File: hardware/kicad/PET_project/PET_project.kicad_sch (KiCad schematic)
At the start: 22 parts, among them J1 Conn_01x02_Socket, J2 Screw_Terminal_01x02, J3 Screw_Terminal_01x02, J4 Conn_01x02_Socket, J5 GY-GPSV2-NEO6M, J6 BMM350, J7 MPU6050, J8 Conn_01x02_Socket, J9 BMP280, Q2 NMOS, Q3 NMOS, U8 BA50DD0T

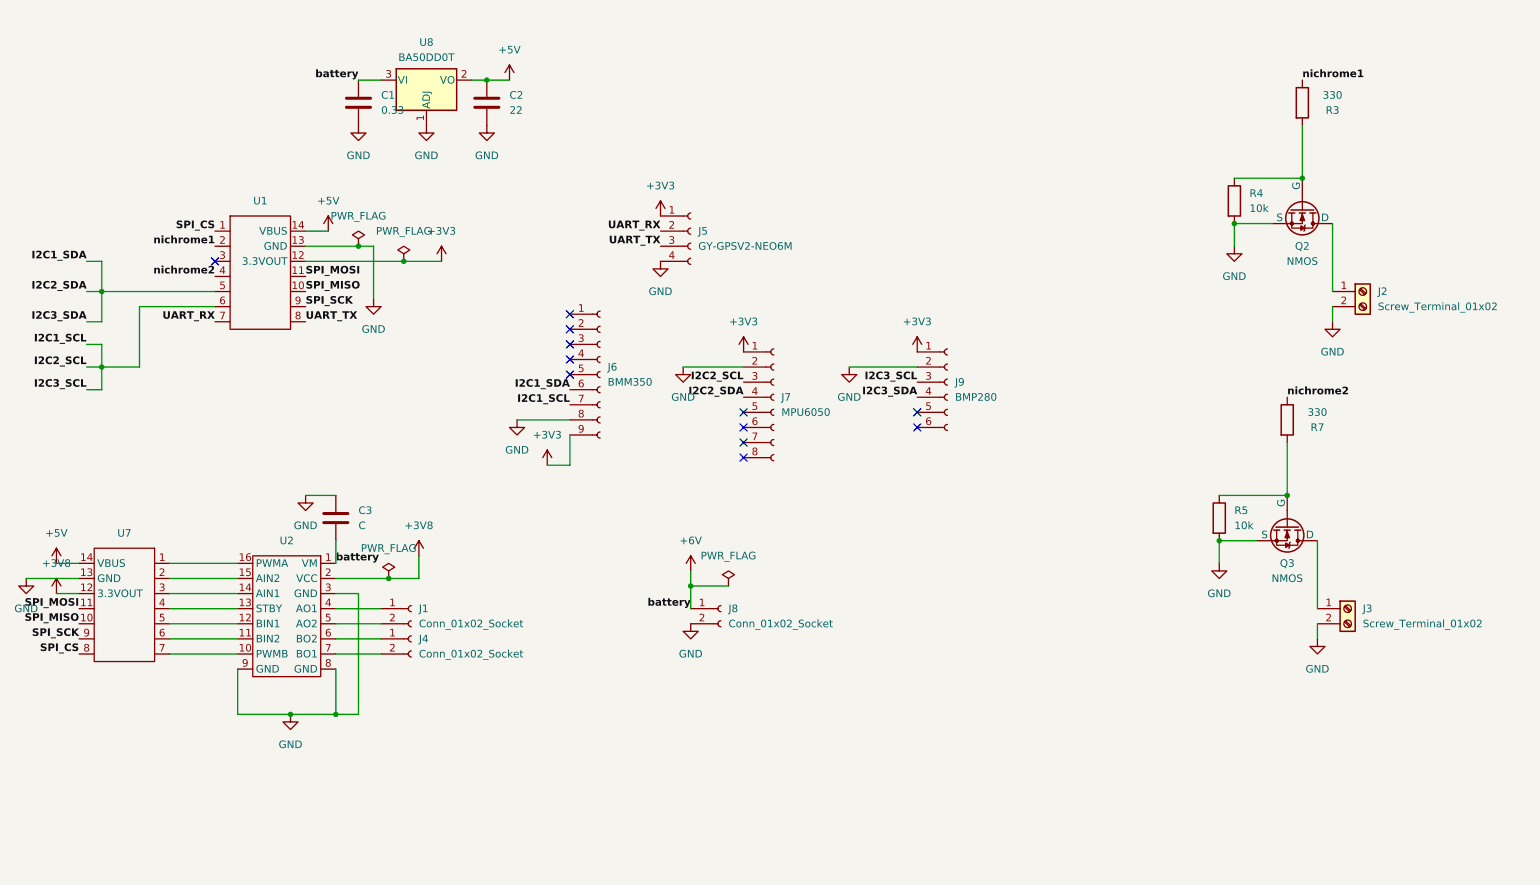
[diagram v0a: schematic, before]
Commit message: 基板設計変更① ・モーター変更によるソケット部分の変更 ・エクスパンサの追加 ・エクスパンサにニクロム、LEDを接続 ・エンコーダー周りの接続 ・地磁気センサの削除 ・xiao2の削除
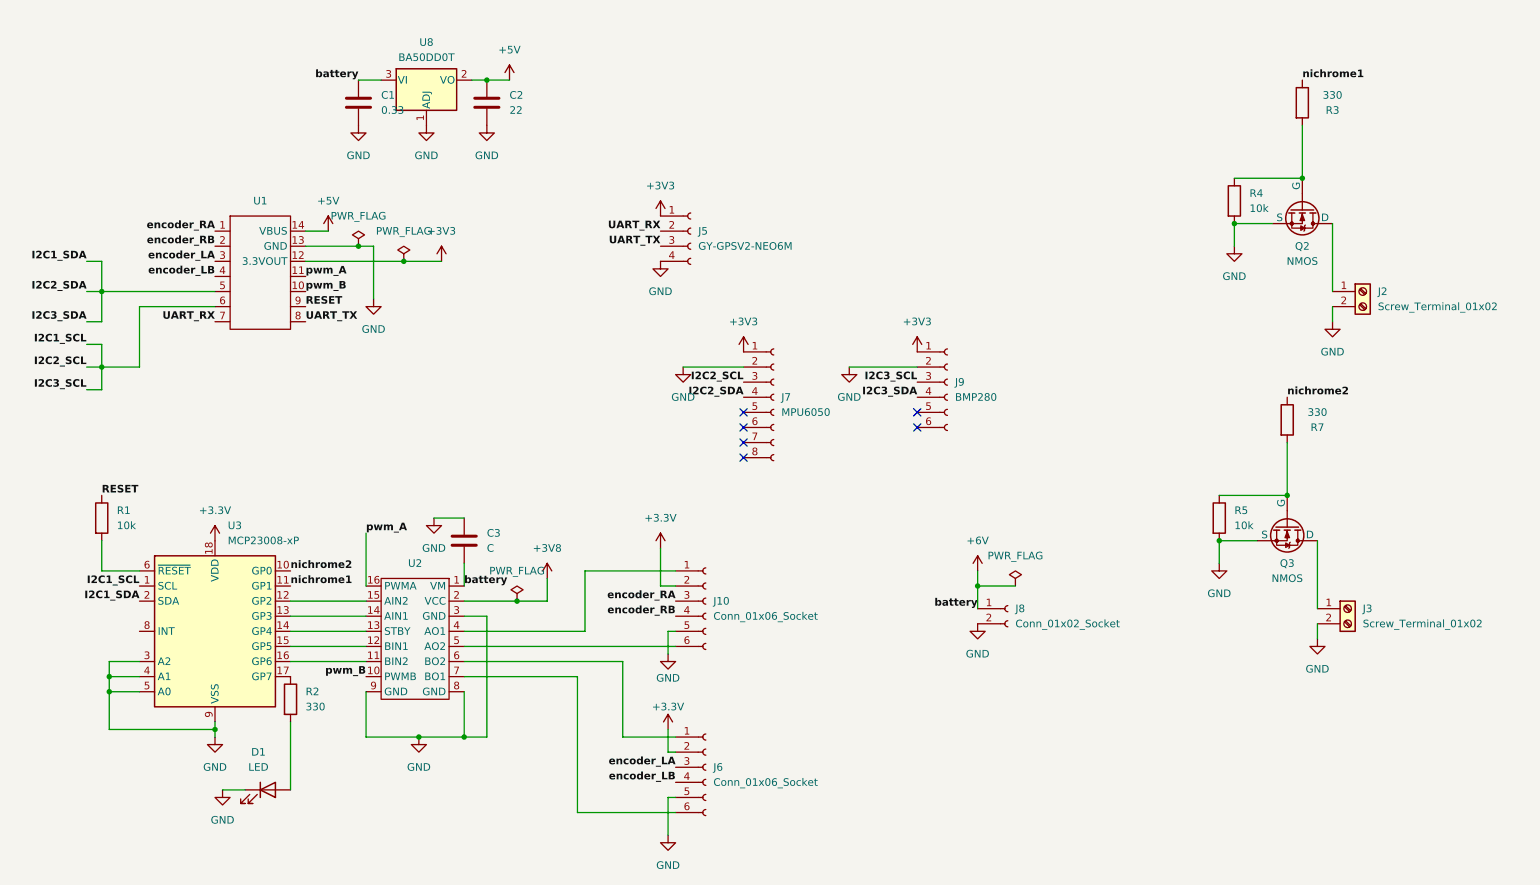
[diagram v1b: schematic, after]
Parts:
- removed J1, J4: Conn_01x02_Socket, Connector_JST:JST_XH_S2B-XH-A_1x02_P2.50mm_Horizontal, symbol Connector:Conn_01x02_Socket
- removed J6: BMM350, my_footprint:BMM350_PinSocket_Vertical, symbol Connector:Conn_01x09_Socket
- removed U7: (no value), my_footprint:XIAO-ESP32-S3-DIP, symbol my_symbol:XIAO_ESP32S3
- added D1: LED, symbol Device:LED
- added J10, J6: Conn_01x06_Socket, symbol Connector:Conn_01x06_Socket
- added R1: 10k, symbol Device:R
- added R2: 330, symbol Device:R
- added U3: MCP23008-xP, Package_DIP:DIP-18_W7.62mm, symbol Interface_Expansion:MCP23008-xP
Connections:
- net SPI_MISO is gone; now on net pwm_B: U1.10
- net SPI_MOSI is gone; now on net pwm_A: U1.11
- net GND: now also D1.1 (K), J10.5 (Pin_5), J6.5 (Pin_5), U3.3 (A2), U3.4 (A1), U3.5 (A0), U3.9 (VSS)
- net I2C1_SCL: now also U3.1 (SCL)
- net I2C1_SDA: now also U3.2 (SDA)
- net nichrome1: now also U3.11 (GP1); no longer U1.2
- net nichrome2: now also U3.10 (GP0); no longer U1.4
- net pwm_B: now reaches U2.10 (PWMB)
- net at U2.11 (BIN2): now also U3.16 (GP6)
- net at U2.12 (BIN1): now also U3.15 (GP5)
- net at U2.13 (STBY): now also U3.14 (GP4)
- net at U2.14 (AIN1): now also U3.13 (GP3)
- net at U2.15 (AIN2): now also U3.12 (GP2)
- net pwm_A: now reaches U2.16 (PWMA)
- net at U2.4 (AO1): now also J10.1 (Pin_1)
- net at U2.5 (AO2): now also J10.6 (Pin_6)
- net at U2.6 (BO2): now also J6.1 (Pin_1)
- net at U2.7 (BO1): now also J6.6 (Pin_6)
- net encoder_LA: now reaches U1.3
- net encoder_LA: now also J6.3 (Pin_3)
- net SPI_CS renamed encoder_RA
- net encoder_RA: now also J10.3 (Pin_3)
- net SPI_SCK renamed RESET
- net RESET: now also R1.1
- new net: R2.1, U3.17 (GP7)
- new net: R1.2, U3.6 (~{RESET})
- new net: D1.2 (A), R2.2
- new net +3.3V: J10.2 (Pin_2), J6.2 (Pin_2), U3.18 (VDD)
- new net encoder_LB: J6.4 (Pin_4), U1.4
- new net encoder_RB: J10.4 (Pin_4), U1.2
- no-connect marks 12 -> 6
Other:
- moved on the sheet: C3, J8, U2

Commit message: 基板設計変更②
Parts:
- removed U8: BA50DD0T, Package_TO_SOT_THT:TO-220-3_Vertical, symbol Regulator_Linear:LM317_TO-220
- added U4: BA50DD0T, Package_TO_SOT_THT:TO-220-3_Vertical, symbol Regulator_Linear:LM7805_TO220
- D1: footprint (none) -> LED_THT:LED_D5.0mm_Clear
- J10, J6: footprint (none) -> Connector_JST:JST_XH_S6B-XH-A-1_1x06_P2.50mm_Horizontal
- R1, R2: footprint (none) -> Resistor_THT:R_Axial_DIN0204_L3.6mm_D1.6mm_P2.54mm_Vertical
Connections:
- net +3.3V is gone; now on net +3V3: J10.2 (Pin_2), J6.2 (Pin_2), U3.18 (VDD)
- net +3V8 is gone; now on net +3V3: U2.2 (VCC)
- net +5V: now also U4.3 (VO)
- net +6V: now also J2.2 (Pin_2), J3.2 (Pin_2), U4.1 (VI)
- net GND: now also U4.2 (GND); no longer J2.2 (Pin_2), J3.2 (Pin_2)
- net encoder_RA: now also U1.2; no longer U1.1
- net encoder_RB: now also U1.1; no longer U1.2
- net pwm_A: now also U1.10; no longer U1.11
- net pwm_B: now also U1.11; no longer U1.10
- no-connect marks 6 -> 7

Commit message: ショットキーバリアダイオード追加
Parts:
- added D2: D_Schottky, my_footprint:D_schottky, symbol Device:D_Schottky
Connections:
- net +5V: now also D2.2 (A); no longer U1.14 (VBUS)
- new net: D2.1 (K), U1.14 (VBUS)
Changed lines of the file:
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@@
 	(wire
 		(pts
+			(xy 66.04 52.07) (xy 66.04 55.88)
+		)
+		(stroke
+			(width 0)
+			(type default)
+		)
+	)
+	(wire
+		(pts
 			(xy 29.21 66.04) (xy 29.21 60.96)
 		)
@@
 	(wire
 		(pts
-			(xy 67.31 55.88) (xy 63.5 55.88)
-		)
-		(stroke
-			(width 0)
-			(type default)
-		)
-	)
-	(wire
-		(pts
 			(xy 90.17 111.76) (xy 90.17 115.57)
 		)
@@
 	(wire
 		(pts
+			(xy 66.04 55.88) (xy 63.5 55.88)
+		)
+		(stroke
+			(width 0)
+			(type default)
+		)
+	)
+	(wire
+		(pts
 			(xy 123.19 109.22) (xy 123.19 115.57)
 		)
@@
 	(symbol
 		(lib_id "power:+5V")
-		(at 67.31 55.88 0)
+		(at 66.04 44.45 0)
 		(unit 1)
 		(body_style 1)
@@
 		(fields_autoplaced yes)
 		(property "Reference" "#PWR014"
-			(at 67.31 59.69 0)
+			(at 66.04 48.26 0)
 			(hide yes)
 			(show_name no)
@@
 		)
 		(property "Value" "+5V"
-			(at 67.31 50.8 0)
+			(at 66.04 39.37 0)
 			(show_name no)
 			(do_not_autoplace no)
@@
 		)
 		(property "Footprint" ""
-			(at 67.31 55.88 0)
+			(at 66.04 44.45 0)
 			(hide yes)
 			(show_name no)
@@
 		)
 		(property "Datasheet" ""
-			(at 67.31 55.88 0)
+			(at 66.04 44.45 0)
 			(hide yes)
 			(show_name no)
@@
 		)
 		(property "Description" "Power symbol creates a global label with name \"+5V\""
-			(at 67.31 55.88 0)
+			(at 66.04 44.45 0)
 			(hide yes)
 			(show_name no)
@@
 					(unit 1)
 				)
+			)
+		)
+	)
+	(symbol
+		(lib_id "Device:D_Schottky")
+		(at 66.04 48.26 90)
+		(unit 1)
+		(body_style 1)
+		(exclude_from_sim no)
+		(in_bom yes)
+		(on_board yes)
+		(in_pos_files yes)
+		(dnp no)
+		(fields_autoplaced yes)
+		(property "Reference" "D2"
+			(at 68.58 47.3074 90)
+			(show_name no)
+			(do_not_autoplace no)
+			(effects
+				(font
+					(size 1.27 1.27)
+				)
+				(justify right)
+			)
+		)
+		(property "Value" "D_Schottky"
+			(at 68.58 49.8474 90)
+			(show_name no)
+			(do_not_autoplace no)
+			(effects
+				(font
+					(size 1.27 1.27)
+				)
+				(justify right)
+			)
+		)
+		(property "Footprint" "my_footprint:D_schottky"
+			(at 66.04 48.26 0)
+			(hide yes)
+			(show_name no)
+			(do_not_autoplace no)
+			(effects
+				(font
+					(size 1.27 1.27)
+				)
+			)
+		)
+		(property "Datasheet" ""
+			(at 66.04 48.26 0)
+			(hide yes)
+			(show_name no)
+			(do_not_autoplace no)
+			(effects
+				(font
+					(size 1.27 1.27)
+				)
+			)
+		)
+		(property "Description" "Schottky diode"
+			(at 66.04 48.26 0)
+			(hide yes)
+			(show_name no)
+			(do_not_autoplace no)
+			(effects
+				(font
+					(size 1.27 1.27)
+				)
+			)
+		)
+		(pin "2"
+		)
+		(pin "1"
+		)
+		(instances
+			(project "PET_project"
+				(path "/de26d571-f6ef-427c-bc25-8e6a6d3b46d4"
+					(reference "D2")
+					(unit 1)
+				)
